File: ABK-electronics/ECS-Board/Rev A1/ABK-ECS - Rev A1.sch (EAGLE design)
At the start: 141 parts, among them J1 1241050-5, J2 USB3075-30-A, J3 22-27-2061-06, J4 22-05-7068-06, J5 22-05-7028-02, J6 22-05-7028-02, J7 22-05-7068-06, K3 G6K-2G-Y, SW1 B3FS-1015, SW2 B3FS-1015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

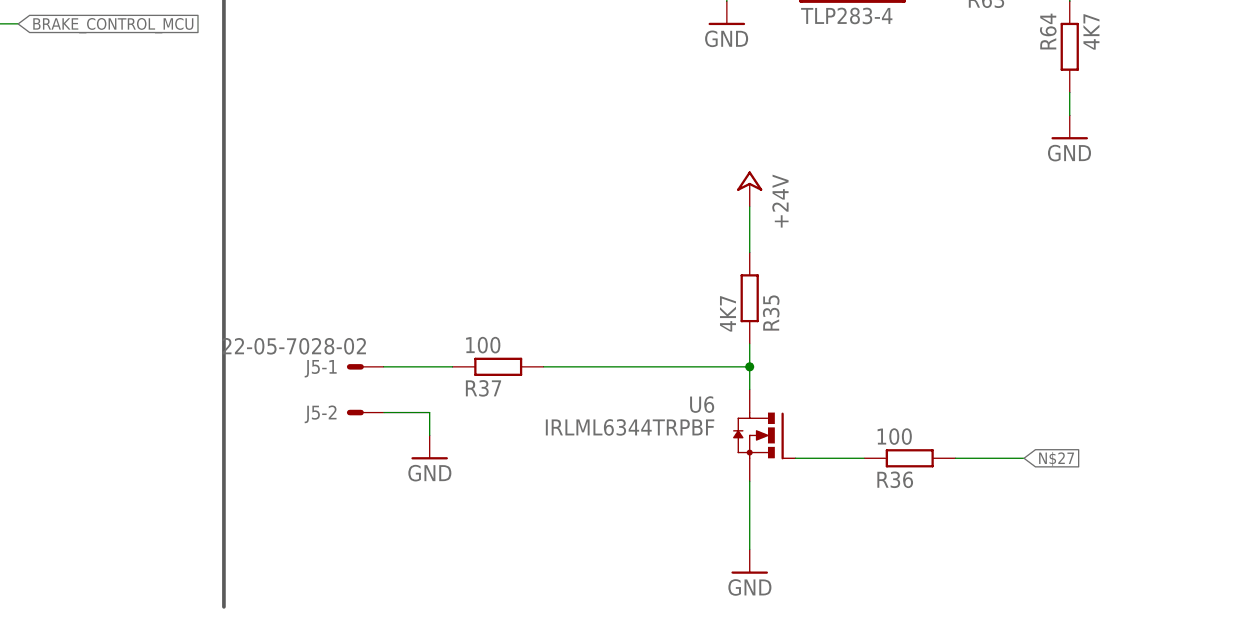
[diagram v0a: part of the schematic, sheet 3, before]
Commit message: Route the board and modify schematic
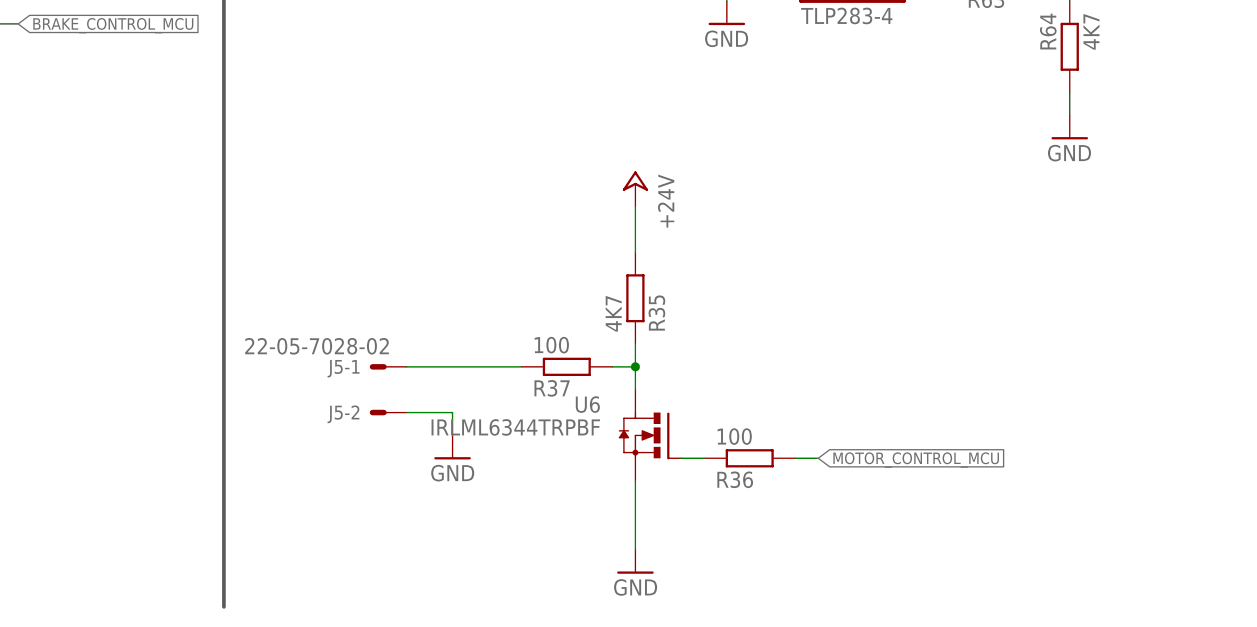
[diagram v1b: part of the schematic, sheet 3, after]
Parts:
- removed C9: 0.1uF, rcl:C-EUC0603
- removed L1: 0603PS-103KLB, coilcraft:0603PS
- J2: value USB3075-30-A -> USB-B-S-RA; device con-GlobalConnectorTechnology:USB3075-30-A -> con-multicomp:USB-B-S-RA; MPN USB3075-30-A -> (none); OC_NEWARK 58T0863 -> (none)
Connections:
- removed net AVDD: C9.1, L1.2, U2.VDDA, U2.VREFP
- removed net N$27: R36.2
- removed net N$58: U2.P1[26]/MCOB1/PWM1[6]/CAP0[0]
- new net 2: MP2.1, SJ5.2
- new net 3: MP3.1, SJ4.2
- new net 4: MP4.1, SJ1.2
- new net MOTOR_CONTROL_MCU: R36.2, U2.P1[26]/MCOB1/PWM1[6]/CAP0[0]
- net +3V3: no longer L1.1
- net 1: no longer MP2.1, MP3.1, MP4.1, SJ1.2, SJ4.2, SJ5.2
- net GND: now also J2.GND, U1.WP; no longer C9.2, J2.5
- net N$1: now also J2.DATA+; no longer J2.2
- net N$2: now also J2.DATA-; no longer J2.3
- net USB_V_BUS: now also J2.VUSB; no longer J2.1
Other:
- note removed: "ADC DECOUPLING"
- moved on the sheet: J5-1, J5-2, R11, R12, R35, R36, R37, SJ1, SJ2, SJ4, SJ5, U6

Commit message: Rename guard ring to GND Put GND via under alim component Add a pull-down to WP on AT24
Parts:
- added R65: 4K7, rcl:R-EU_R0603
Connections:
- new net N$27: R65.1, U1.WP
- net GND: now also R65.2; no longer U1.WP
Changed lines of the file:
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@@
 <part name="GND69" library="supply1" deviceset="GND" device=""/>
 <part name="J2" library="con-multicomp" deviceset="USB-B-S-RA" device=""/>
+<part name="R65" library="rcl" deviceset="R-EU_" device="R0603" value="4K7">
+<attribute name="MF" value=""/>
+<attribute name="MPN" value="MCMR06X4701FTL"/>
+<attribute name="OC_NEWARK" value="86T3649"/>
+</part>
 </parts>
 <sheets>
@@
 <instance part="GND20" gate="1" x="370.84" y="33.02"/>
 <instance part="J2" gate="G$1" x="195.58" y="43.18"/>
+<instance part="R65" gate="G$1" x="24.13" y="17.78" rot="R270">
+<attribute name="OC_NEWARK" x="24.13" y="17.78" size="1.778" layer="96" rot="R180" display="off"/>
+<attribute name="MF" x="24.13" y="17.78" size="1.778" layer="96" rot="R180" display="off"/>
+<attribute name="MPN" x="24.13" y="17.78" size="1.778" layer="96" rot="R180" display="off"/>
+</instance>
 </instances>
 <busses>
@@
 <pinref part="GND7" gate="1" pin="GND"/>
 <wire x1="41.91" y1="20.32" x2="31.75" y2="20.32" width="0.1524" layer="91"/>
-<wire x1="31.75" y1="20.32" x2="31.75" y2="10.16" width="0.1524" layer="91"/>
+<wire x1="31.75" y1="20.32" x2="31.75" y2="11.43" width="0.1524" layer="91"/>
 <pinref part="U1" gate="A" pin="A0"/>
+<wire x1="31.75" y1="11.43" x2="31.75" y2="10.16" width="0.1524" layer="91"/>
 <wire x1="41.91" y1="35.56" x2="31.75" y2="35.56" width="0.1524" layer="91"/>
 <wire x1="31.75" y1="35.56" x2="31.75" y2="33.02" width="0.1524" layer="91"/>
@@
 <pinref part="U1" gate="A" pin="A1"/>
 <wire x1="31.75" y1="33.02" x2="31.75" y2="30.48" width="0.1524" layer="91"/>
-<wire x1="31.75" y1="30.48" x2="31.75" y2="25.4" width="0.1524" layer="91"/>
-<wire x1="31.75" y1="25.4" x2="31.75" y2="20.32" width="0.1524" layer="91"/>
+<wire x1="31.75" y1="30.48" x2="31.75" y2="20.32" width="0.1524" layer="91"/>
 <wire x1="41.91" y1="33.02" x2="31.75" y2="33.02" width="0.1524" layer="91"/>
 <junction x="31.75" y="33.02"/>
@@
 <wire x1="41.91" y1="30.48" x2="31.75" y2="30.48" width="0.1524" layer="91"/>
 <junction x="31.75" y="30.48"/>
-<pinref part="U1" gate="A" pin="WP"/>
-<wire x1="41.91" y1="25.4" x2="31.75" y2="25.4" width="0.1524" layer="91"/>
-<junction x="31.75" y="25.4"/>
+<pinref part="R65" gate="G$1" pin="2"/>
+<wire x1="24.13" y1="12.7" x2="24.13" y2="11.43" width="0.1524" layer="91"/>
+<wire x1="24.13" y1="11.43" x2="31.75" y2="11.43" width="0.1524" layer="91"/>
+<junction x="31.75" y="11.43"/>
 </segment>
 <segment>
@@
 </segment>
 </net>
+<net name="N$27" class="0">
+<segment>
+<wire x1="41.91" y1="25.4" x2="24.13" y2="25.4" width="0.1524" layer="91"/>
+<wire x1="24.13" y1="25.4" x2="24.13" y2="22.86" width="0.1524" layer="91"/>
+<pinref part="R65" gate="G$1" pin="1"/>
+<pinref part="U1" gate="A" pin="WP"/>
+</segment>
+</net>

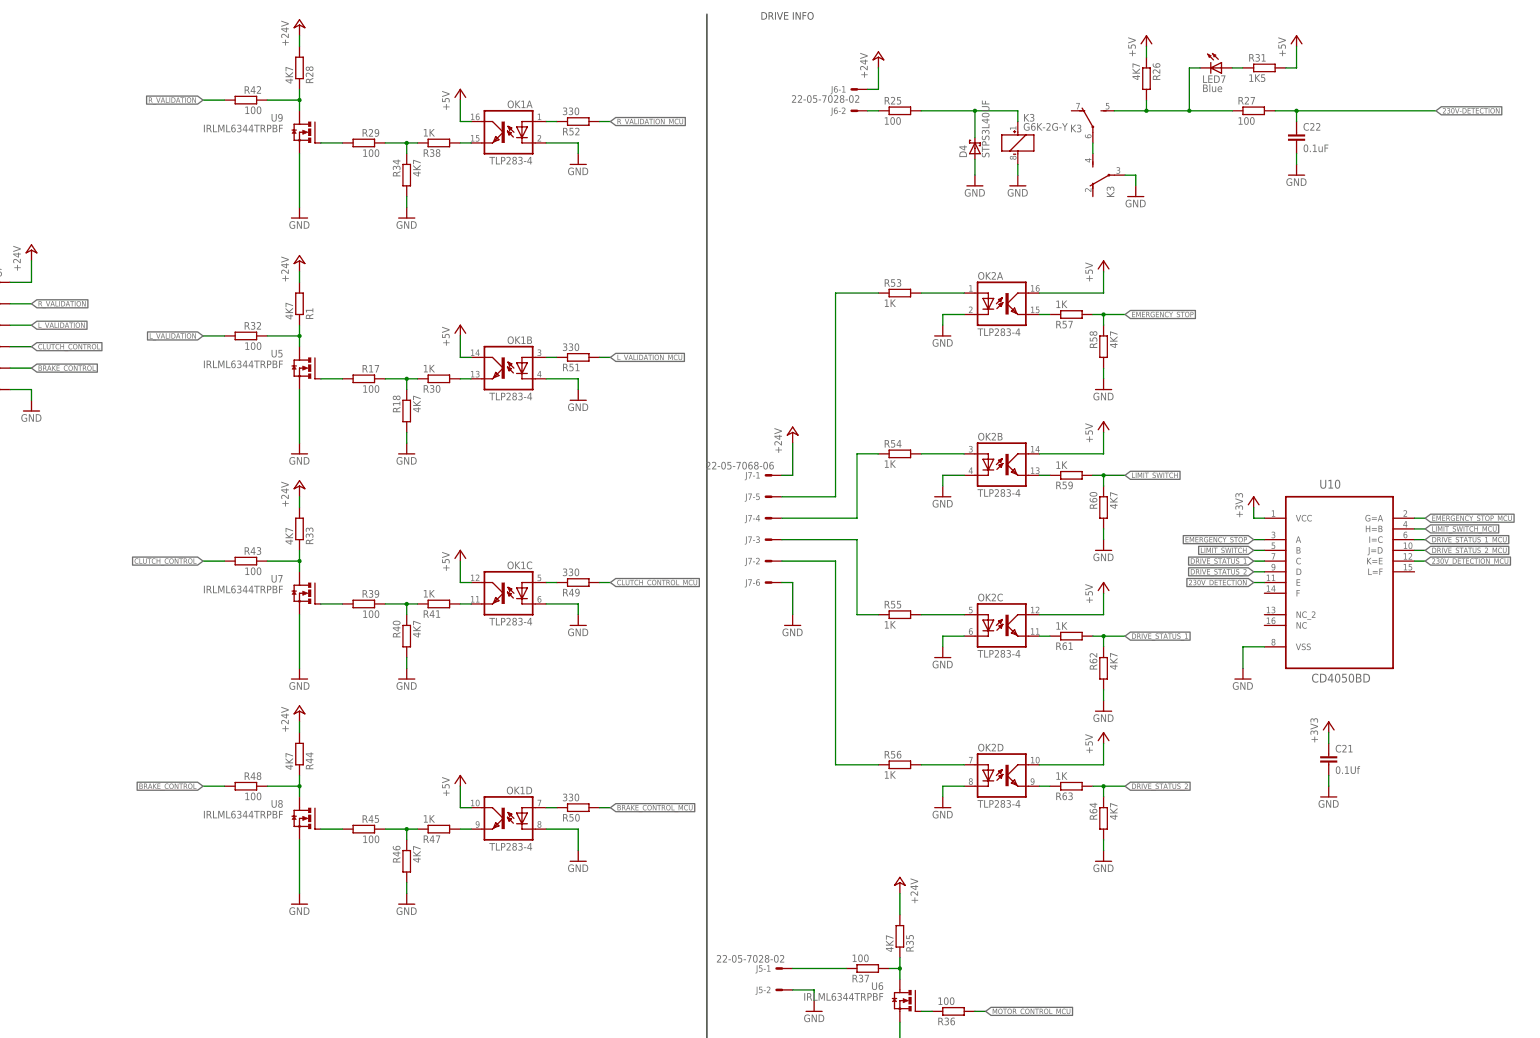
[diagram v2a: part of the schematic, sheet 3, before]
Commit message: Add LEDs on input and output
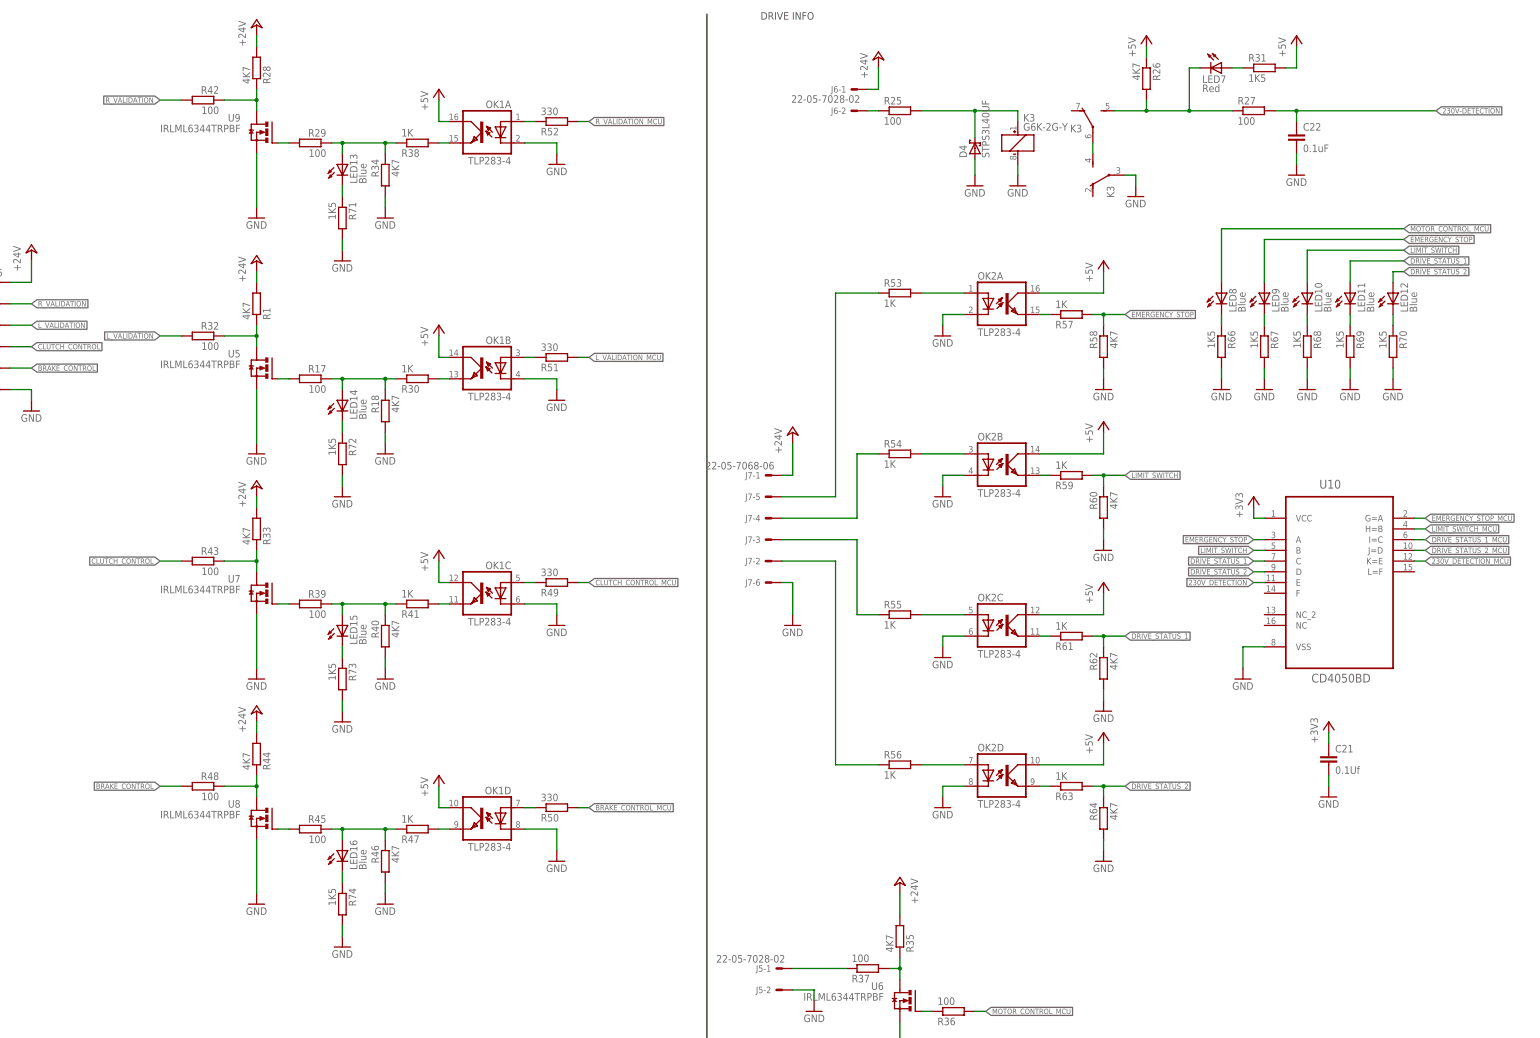
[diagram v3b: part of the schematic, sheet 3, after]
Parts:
- added LED10, LED11, LED12, LED13, LED14, LED15, LED16, LED8, LED9: Blue, led:LEDCHIPLED_0603
- added R66, R67, R68, R69, R70, R71, R72, R73, R74: 1K5, rcl:R-EU_R0603
- LED7: value Blue -> Red
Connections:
- new net N$56: LED8.C, R66.1
- new net N$57: LED9.C, R67.1
- new net N$58: LED10.C, R68.1
- new net N$59: LED11.C, R69.1
- new net N$65: LED12.C, R70.1
- new net N$66: LED13.C, R71.1
- new net N$67: LED14.C, R72.1
- new net N$68: LED15.C, R73.1
- new net N$69: LED16.C, R74.1
- net 230V-DETECTION: now also U2.P1[27]/CLKOUT/*USB_OVRCR/CAP0[1]
- net DRIVE_STATUS_1: now also LED11.A
- net DRIVE_STATUS_2: now also LED12.A
- net EMERGENCY_STOP: now also LED9.A
- net GND: now also R66.2, R67.2, R68.2, R69.2, R70.2, R71.2, R72.2, R73.2, R74.2
- net LIMIT_SWITCH: now also LED10.A
- net MOTOR_CONTROL_MCU: now also LED8.A
- net N$20: now also LED13.A
- net N$25: now also LED14.A
- net N$34: now also LED15.A
- net N$37: now also LED16.A
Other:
- moved on the sheet: OK1A, OK1B, OK1C, OK1D, R1, R17, R18, R28, R29, R30, R32, R33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

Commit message: Add component reference
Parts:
- C21: MPN (none) -> MC0603B104K500CT; OC_NEWARK (none) -> 06R4927
- C22: MPN MC0603B104K250CT -> MC0603B104K160CT; OC_NEWARK 06R4925 -> 06R4923
- CC1, JP1, JP2, JP3, JP4, MP1, MP2, MP3, MP4, SJ1, SJ2, SJ4, SJ5, T1: OC_NEWARK (none) -> unknown
- J2: MPN (none) -> USB-B-S-RA; OC_NEWARK (none) -> 14N8154
- J4, J7: MPN (none) -> 22-05-7068; OC_NEWARK (none) -> 25M1733
- J5: MPN (none) -> 22-05-7028; OC_NEWARK (none) -> 25M1728
- LED2: value Blue -> Red
- LED5, LED6: MPN OVS-0604 -> OVS-0603; OC_NEWARK 15R2206 -> 15R2205
- OK1, OK2: MF (none) -> VISHAY/TELEFUNKEN; MPN (none) -> TCMT4100; OC_NEWARK (none) -> 06H1639
- R1, R18, R28, R33, R34, R35, R40, R44, R46, R58, R60, R62, R64: MPN MCMR06X1000FTL -> MCMR06X4701FTL; OC_NEWARK 86T3504 -> 86T3649
- R15, R16: value 1k5 -> 1K5; MF Multicomp Passives -> (none); MPN MC0063W060311K5 -> MCMR06X1501FTL; OC_NEWARK 58K4488 -> 86T3542
- R19, R20, R24: value 31k6 -> 31K6; MF Multicomp Passives -> (none); MPN MC0063W060311K5 -> MCMR06X3162FTL; OC_NEWARK 58K4488 -> 86T3613
- R21, R23: value 10k -> 10K
- R22: value 52k3 -> 52K3
- R30, R38, R41, R47, R53, R54, R55, R56, R57, R59, R61, R63: MPN MCMR06X1000FTL -> MCMR06X1001FTL; OC_NEWARK 86T3504 -> 86T3505
- R4, R5: value 4k7 -> 4K7
- R49, R50, R51, R52: MPN MCMR06X1000FTL -> MCMR06X3300FTL; OC_NEWARK 86T3504 -> 86T3616
- SW1, SW2: MPN (none) -> B3FS-1010; OC_NEWARK unknown -> 36M3638

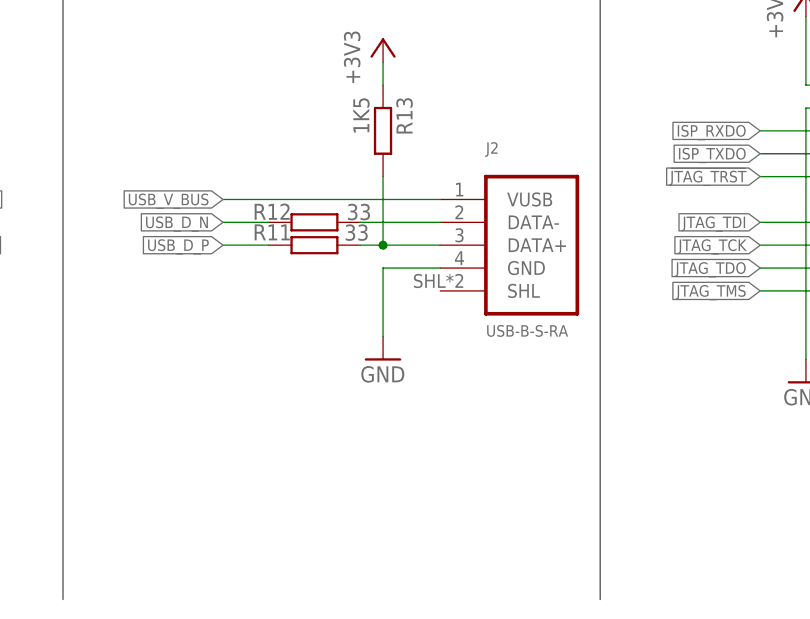
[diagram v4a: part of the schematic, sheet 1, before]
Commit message: Add solderJump to the usb shield and replace layer 3 into 15
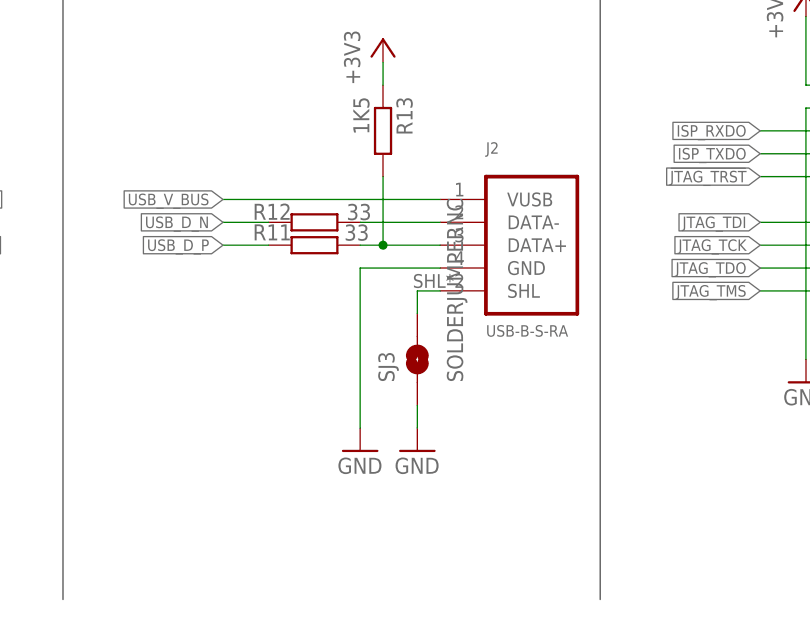
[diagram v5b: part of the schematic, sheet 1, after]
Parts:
- added SJ3: SOLDERJUMPERNC, SparkFun-Passives:SOLDERJUMPERNC
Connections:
- new net N$70: J2.SHL, SJ3.2
- net GND: now also SJ3.1
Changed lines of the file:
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@@
 </part>
 <part name="GND8" library="supply1" deviceset="GND" device=""/>
+<part name="SJ3" library="SparkFun-Passives" deviceset="SOLDERJUMPER" device="NC"/>
+<part name="GND78" library="supply1" deviceset="GND" device=""/>
 </parts>
 <sheets>
@@
 <attribute name="MPN" x="176.53" y="45.72" size="1.778" layer="96" display="off"/>
 </instance>
-<instance part="GND17" gate="1" x="184.15" y="30.48"/>
+<instance part="GND17" gate="1" x="181.61" y="20.32"/>
 <instance part="R13" gate="G$1" x="184.15" y="55.88" rot="R270">
 <attribute name="OC_NEWARK" x="184.15" y="55.88" size="1.778" layer="96" display="off"/>
@@
 <attribute name="MPN" x="24.13" y="17.78" size="1.778" layer="96" rot="R180" display="off"/>
 </instance>
+<instance part="SJ3" gate="1" x="187.96" y="30.48" rot="R90"/>
+<instance part="GND78" gate="1" x="187.96" y="20.32"/>
 </instances>
 <busses>
@@
 <segment>
 <pinref part="GND17" gate="1" pin="GND"/>
-<wire x1="184.15" y1="40.64" x2="184.15" y2="33.02" width="0.1524" layer="91"/>
+<wire x1="181.61" y1="40.64" x2="181.61" y2="22.86" width="0.1524" layer="91"/>
 <pinref part="J2" gate="G$1" pin="GND"/>
-<wire x1="190.5" y1="40.64" x2="184.15" y2="40.64" width="0.1524" layer="91"/>
+<wire x1="190.5" y1="40.64" x2="181.61" y2="40.64" width="0.1524" layer="91"/>
 </segment>
 <segment>
@@
 <pinref part="R14" gate="G$1" pin="2"/>
 <wire x1="370.84" y1="35.56" x2="370.84" y2="38.1" width="0.1524" layer="91"/>
+</segment>
+<segment>
+<pinref part="SJ3" gate="1" pin="1"/>
+<wire x1="187.96" y1="22.86" x2="187.96" y2="25.4" width="0.1524" layer="91"/>
+<pinref part="GND78" gate="1" pin="GND"/>
 </segment>
 </net>
@@
 </segment>
 </net>
+<net name="N$70" class="0">
+<segment>
+<pinref part="SJ3" gate="1" pin="2"/>
+<pinref part="J2" gate="G$1" pin="SHL"/>
+<wire x1="187.96" y1="35.56" x2="187.96" y2="38.1" width="0.1524" layer="91"/>
+<wire x1="187.96" y1="38.1" x2="190.5" y2="38.1" width="0.1524" layer="91"/>
+</segment>
+</net>
